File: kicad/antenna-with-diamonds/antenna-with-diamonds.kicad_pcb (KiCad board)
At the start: 4 copper layers, 25 x 20 mm, 2 parts, among them J101 SMA-elbowed_amplified-RF-input

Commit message: Changed stackup to 2 layers
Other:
- copper layers 4 -> 2
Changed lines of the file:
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@@
 	(generator_version "9.0")
 	(general
-		(thickness 1.6062)
+		(thickness 1.6)
 		(legacy_teardrops no)
 	)
 	(paper "A4")
 	(layers
-		(0 "F.Cu" signal)
-		(4 "In1.Cu" signal)
-		(6 "In2.Cu" signal)
-		(2 "B.Cu" signal)
+		(0 "F.Cu" mixed)
+		(2 "B.Cu" mixed)
 		(9 "F.Adhes" user "F.Adhesive")
 		(11 "B.Adhes" user "B.Adhesive")
@@
 			(layer "F.Mask"
 				(type "Top Solder Mask")
-				(color "Green")
 				(thickness 0.01)
 			)
@@
 			)
 			(layer "dielectric 1"
-				(type "prepreg")
-				(thickness 0.2104)
-				(material "FR4")
-				(epsilon_r 4.5)
-				(loss_tangent 0.02)
-			)
-			(layer "In1.Cu"
-				(type "copper")
-				(thickness 0.0152)
-			)
-			(layer "dielectric 2"
 				(type "core")
-				(thickness 1.065)
-				(material "FR4")
-				(epsilon_r 4.5)
-				(loss_tangent 0.02)
-			)
-			(layer "In2.Cu"
-				(type "copper")
-				(thickness 0.0152)
-			)
-			(layer "dielectric 3"
-				(type "prepreg")
-				(thickness 0.2104)
+				(thickness 1.51)
 				(material "FR4")
 				(epsilon_r 4.5)
@@
 			(layer "B.Mask"
 				(type "Bottom Solder Mask")
-				(color "Green")
 				(thickness 0.01)
 			)
@@
 				(type "Bottom Silk Screen")
 			)
-			(copper_finish "HAL lead-free")
+			(copper_finish "None")
 			(dielectric_constraints no)
 		)

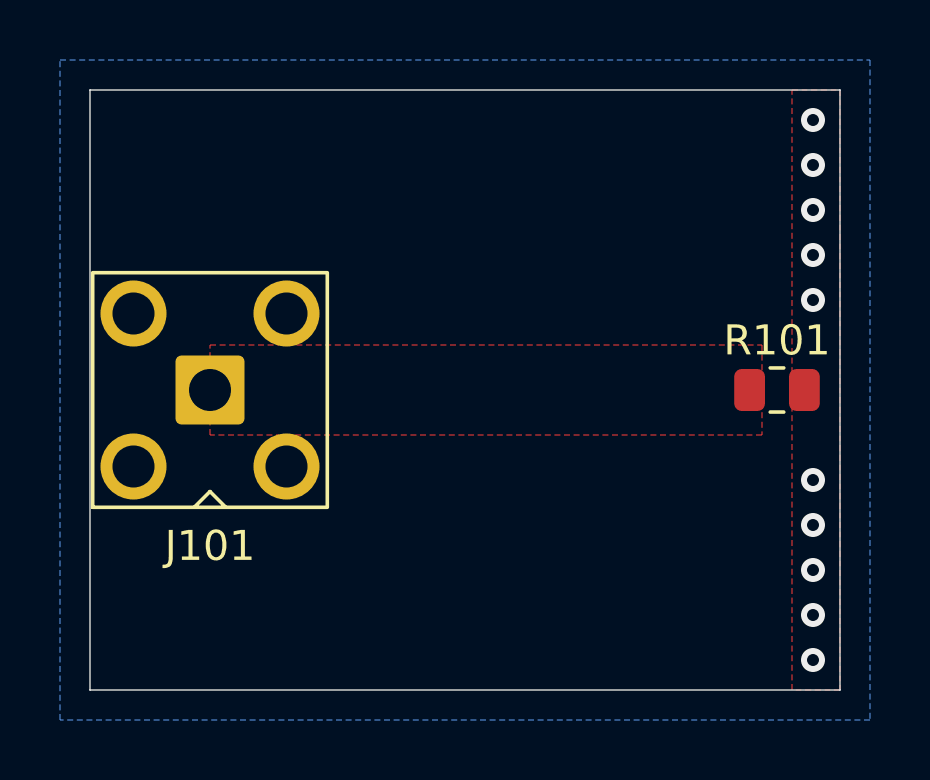
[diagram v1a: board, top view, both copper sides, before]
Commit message: Finished silkscreen of antenna
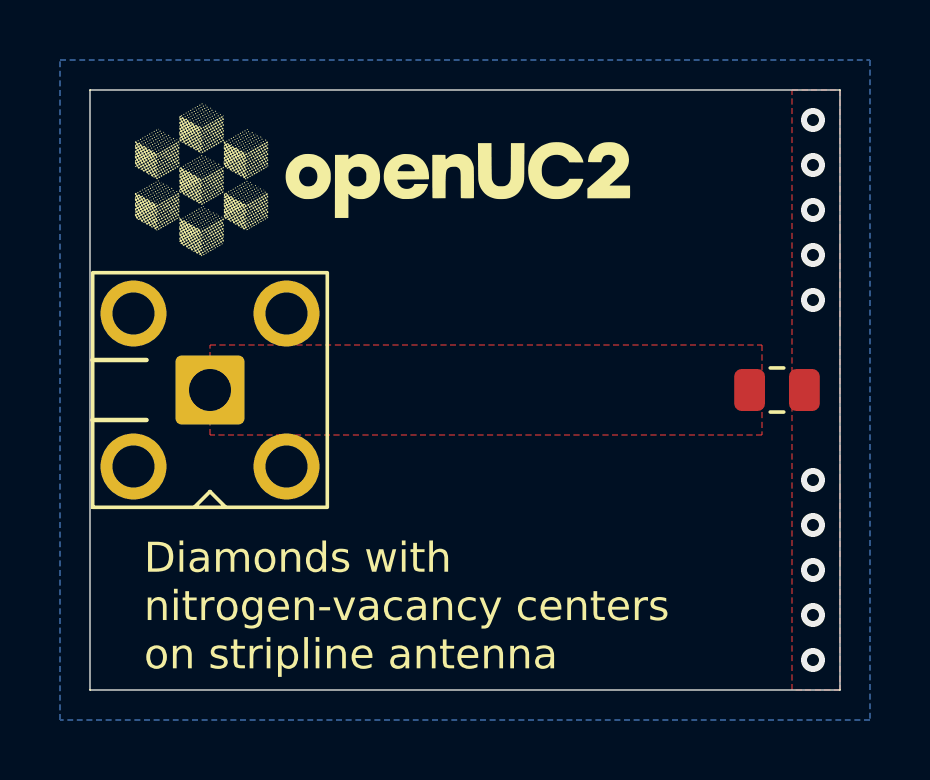
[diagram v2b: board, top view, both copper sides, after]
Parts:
- added G***: LOGO, logos:uc2-hexa-cubes_coarse_5mm, B.Cu at (121.0, 104.0)
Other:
- board text added: "Diamonds with nitrogen-vacancy centers on stripline antenna"
- board text added: "antenna-with-diamonds christiankuttke 2025-09-22; Rev. A openUC2 GmbH"
